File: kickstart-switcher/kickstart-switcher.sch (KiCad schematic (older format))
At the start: 13 parts, among them P1 CONN_01X04, Q1 Q_NMOS_GSD, U1 74HC74, U2 74HC14

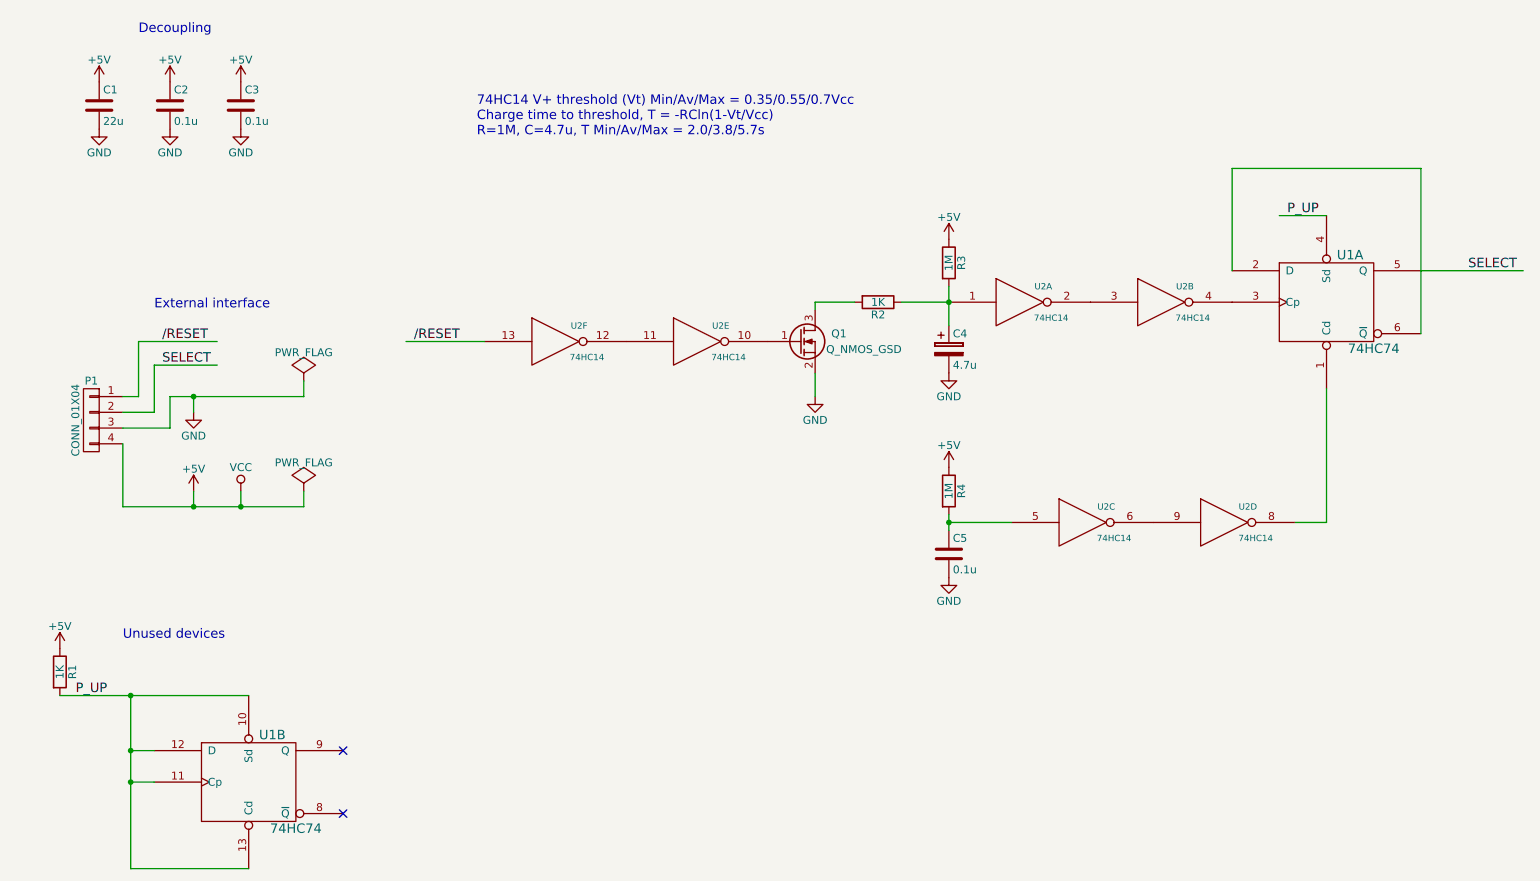
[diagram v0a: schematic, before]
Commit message: kickstart-switcher: Add 1K protection resistors to RC delay HCMOS inputs. Prevents excessive current through over-voltage diodes on power down.
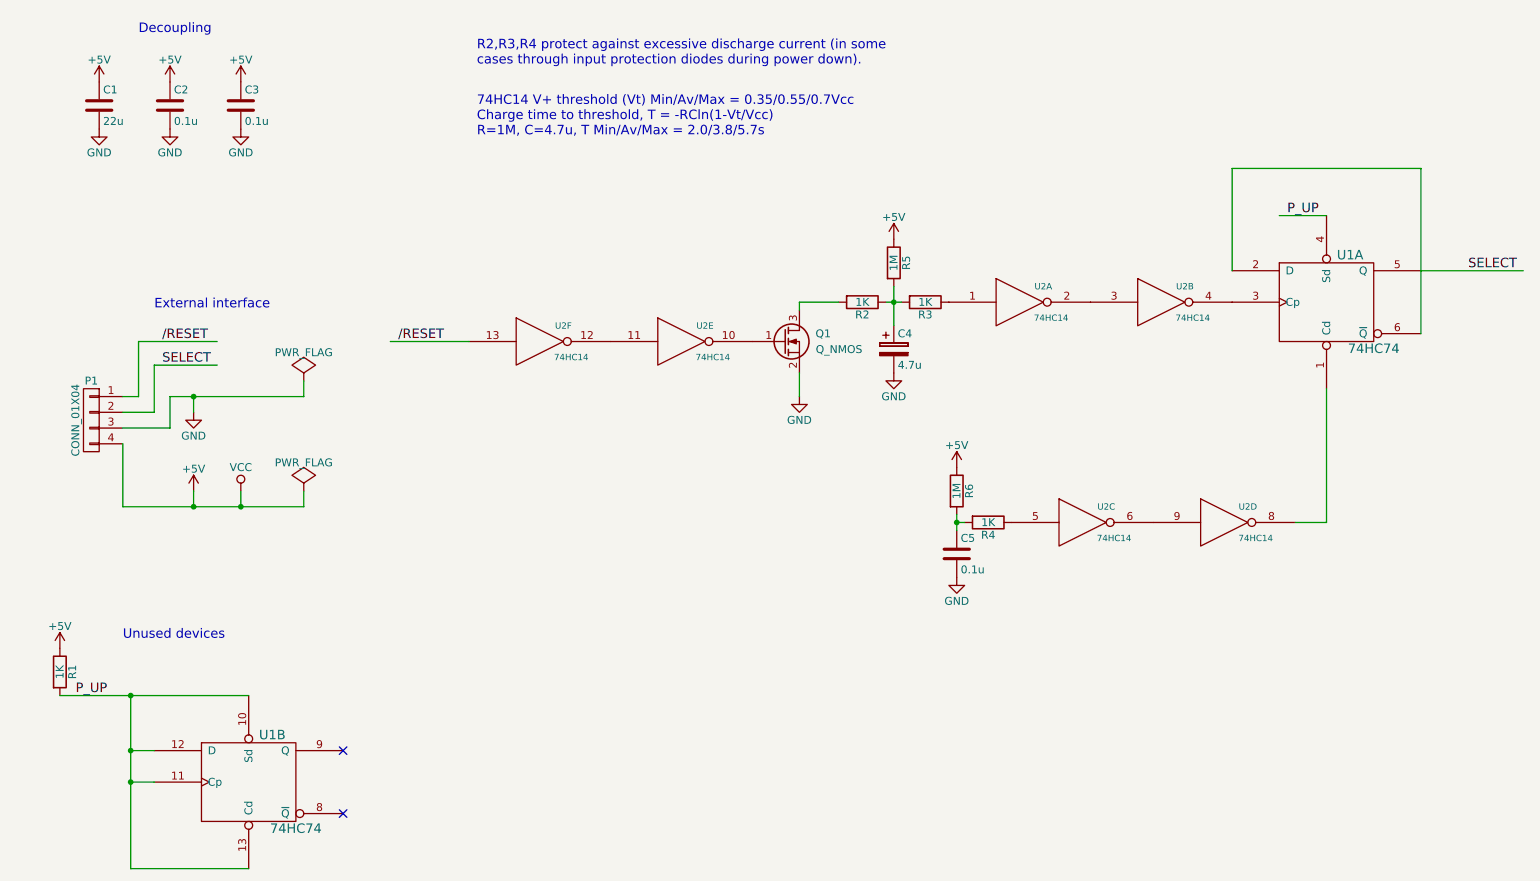
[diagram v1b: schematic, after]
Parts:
- added R3, R4: 1K, Resistors_SMD:R_0805_HandSoldering, symbol R
- Q1: value Q_NMOS_GSD -> Q_NMOS
- renumbered R3 to R5, R4 to R6
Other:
- note added: "R2,R3,R4 protect against excessive discharge current (in some\ncases through input protection diodes during power down)."
- moved on the sheet: C4, C5, Q1, R2, R5, R6, U2E, U2F
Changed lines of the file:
@@
 L +5V #PWR01
 U 1 1 57164698
-P 7150 4250
-F 0 "#PWR01" H 7150 4100 50  0001 C CNN
-F 1 "+5V" H 7150 4390 50  0000 C CNN
-F 2 "" H 7150 4250 60  0000 C CNN
-F 3 "" H 7150 4250 60  0000 C CNN
-	1    7150 4250
+P 7200 4250
+F 0 "#PWR01" H 7200 4100 50  0001 C CNN
+F 1 "+5V" H 7200 4390 50  0000 C CNN
+F 2 "" H 7200 4250 60  0000 C CNN
+F 3 "" H 7200 4250 60  0000 C CNN
+	1    7200 4250
 	1    0    0    -1
 $EndComp
@@
 L GND #PWR02
 U 1 1 571646AB
-P 7150 4950
-F 0 "#PWR02" H 7150 4700 50  0001 C CNN
-F 1 "GND" H 7150 4800 50  0000 C CNN
-F 2 "" H 7150 4950 60  0000 C CNN
-F 3 "" H 7150 4950 60  0000 C CNN
-	1    7150 4950
+P 7200 4950
+F 0 "#PWR02" H 7200 4700 50  0001 C CNN
+F 1 "GND" H 7200 4800 50  0000 C CNN
+F 2 "" H 7200 4950 60  0000 C CNN
+F 3 "" H 7200 4950 60  0000 C CNN
+	1    7200 4950
 	1    0    0    -1
 $EndComp
@@
 L GND #PWR03
 U 1 1 57164A5D
-P 6300 3800
-F 0 "#PWR03" H 6300 3550 50  0001 C CNN
-F 1 "GND" H 6300 3650 50  0000 C CNN
-F 2 "" H 6300 3800 60  0000 C CNN
-F 3 "" H 6300 3800 60  0000 C CNN
-	1    6300 3800
-	1    0    0    -1
-$EndComp
-$Comp
-L R R4
+P 6200 3800
+F 0 "#PWR03" H 6200 3550 50  0001 C CNN
+F 1 "GND" H 6200 3650 50  0000 C CNN
+F 2 "" H 6200 3800 60  0000 C CNN
+F 3 "" H 6200 3800 60  0000 C CNN
+	1    6200 3800
+	1    0    0    -1
+$EndComp
+$Comp
+L R R6
 U 1 1 57164D81
-P 7150 4400
-F 0 "R4" V 7230 4400 50  0000 C CNN
-F 1 "1M" V 7150 4400 50  0000 C CNN
-F 2 "Resistors_SMD:R_0805_HandSoldering" V 7080 4400 30  0001 C CNN
-F 3 "" H 7150 4400 30  0000 C CNN
-	1    7150 4400
+P 7200 4400
+F 0 "R6" V 7280 4400 50  0000 C CNN
+F 1 "1M" V 7200 4400 50  0000 C CNN
+F 2 "Resistors_SMD:R_0805_HandSoldering" V 7130 4400 30  0001 C CNN
+F 3 "" H 7200 4400 30  0000 C CNN
+	1    7200 4400
 	1    0    0    -1
 $EndComp
@@
 L C C5
 U 1 1 57164DA8
-P 7150 4800
-F 0 "C5" H 7175 4900 50  0000 L CNN
-F 1 "0.1u" H 7175 4700 50  0000 L CNN
-F 2 "Resistors_SMD:R_0805_HandSoldering" H 7188 4650 30  0001 C CNN
-F 3 "" H 7150 4800 60  0000 C CNN
-	1    7150 4800
+P 7200 4800
+F 0 "C5" H 7225 4900 50  0000 L CNN
+F 1 "0.1u" H 7225 4700 50  0000 L CNN
+F 2 "Resistors_SMD:R_0805_HandSoldering" H 7238 4650 30  0001 C CNN
+F 3 "" H 7200 4800 60  0000 C CNN
+	1    7200 4800
 	1    0    0    -1
 $EndComp
@@
 L CP C4
 U 1 1 57164E15
-P 7150 3500
-F 0 "C4" H 7175 3600 50  0000 L CNN
-F 1 "4.7u" H 7175 3400 50  0000 L CNN
-F 2 "Resistors_SMD:R_0805_HandSoldering" H 7188 3350 30  0001 C CNN
-F 3 "" H 7150 3500 60  0000 C CNN
-	1    7150 3500
-	1    0    0    -1
-$EndComp
-$Comp
-L R R3
+P 6800 3500
+F 0 "C4" H 6825 3600 50  0000 L CNN
+F 1 "4.7u" H 6825 3400 50  0000 L CNN
+F 2 "Resistors_SMD:R_0805_HandSoldering" H 6838 3350 30  0001 C CNN
+F 3 "" H 6800 3500 60  0000 C CNN
+	1    6800 3500
+	1    0    0    -1
+$EndComp
+$Comp
+L R R5
 U 1 1 57164E66
-P 7150 2950
-F 0 "R3" V 7230 2950 50  0000 C CNN
-F 1 "1M" V 7150 2950 50  0000 C CNN
-F 2 "Resistors_SMD:R_0805_HandSoldering" V 7080 2950 30  0001 C CNN
-F 3 "" H 7150 2950 30  0000 C CNN
-	1    7150 2950
+P 6800 2950
+F 0 "R5" V 6880 2950 50  0000 C CNN
+F 1 "1M" V 6800 2950 50  0000 C CNN
+F 2 "Resistors_SMD:R_0805_HandSoldering" V 6730 2950 30  0001 C CNN
+F 3 "" H 6800 2950 30  0000 C CNN
+	1    6800 2950
 	1    0    0    -1
 $EndComp
@@
 L +5V #PWR04
 U 1 1 57164F16
-P 7150 2800
-F 0 "#PWR04" H 7150 2650 50  0001 C CNN
-F 1 "+5V" H 7150 2940 50  0000 C CNN
-F 2 "" H 7150 2800 60  0000 C CNN
-F 3 "" H 7150 2800 60  0000 C CNN
-	1    7150 2800
+P 6800 2800
+F 0 "#PWR04" H 6800 2650 50  0001 C CNN
+F 1 "+5V" H 6800 2940 50  0000 C CNN
+F 2 "" H 6800 2800 60  0000 C CNN
+F 3 "" H 6800 2800 60  0000 C CNN
+	1    6800 2800
 	1    0    0    -1
 $EndComp
@@
 L GND #PWR05
 U 1 1 57164F39
-P 7150 3650
-F 0 "#PWR05" H 7150 3400 50  0001 C CNN
-F 1 "GND" H 7150 3500 50  0000 C CNN
-F 2 "" H 7150 3650 60  0000 C CNN
-F 3 "" H 7150 3650 60  0000 C CNN
-	1    7150 3650
+P 6800 3650
+F 0 "#PWR05" H 6800 3400 50  0001 C CNN
+F 1 "GND" H 6800 3500 50  0000 C CNN
+F 2 "" H 6800 3650 60  0000 C CNN
+F 3 "" H 6800 3650 60  0000 C CNN
+	1    6800 3650
 	1    0    0    -1
 $EndComp
@@
 NoConn ~ 3300 6050
 NoConn ~ 3300 6450
-Text Label 3750 3450 0    60   ~ 0
+Text Label 3650 3450 0    60   ~ 0
 /RESET
 Text Label 10450 3000 0    60   ~ 0
@@
 $EndComp
 Wire Wire Line
-	7150 4550 7150 4650
-Wire Wire Line
-	7150 4600 7550 4600
-Connection ~ 7150 4600
-Wire Wire Line
-	6300 3650 6300 3800
-Wire Wire Line
-	7150 3100 7150 3350
-Connection ~ 7150 3200
+	7200 4550 7200 4650
+Connection ~ 7200 4600
+Wire Wire Line
+	6200 3650 6200 3800
+Wire Wire Line
+	6800 3100 6800 3350
+Connection ~ 6800 3200
 Wire Wire Line
 	1950 6800 2700 6800
@@
 	9550 2650 9250 2650
 Wire Wire Line
-	4200 3450 3700 3450
+	4100 3450 3600 3450
 Wire Wire Line
 	10150 3000 10800 3000
@@
 L Q_NMOS_GSD Q1
 U 1 1 57188628
-P 6200 3450
-F 0 "Q1" H 6500 3500 50  0000 R CNN
-F 1 "Q_NMOS_GSD" H 6850 3400 50  0000 R CNN
-F 2 "TO_SOT_Packages_SMD:SOT-23_Handsoldering" H 6400 3550 29  0001 C CNN
-F 3 "" H 6200 3450 60  0000 C CNN
-	1    6200 3450
+P 6100 3450
+F 0 "Q1" H 6400 3500 50  0000 R CNN
+F 1 "Q_NMOS" H 6600 3400 50  0000 R CNN
+F 2 "TO_SOT_Packages_SMD:SOT-23_Handsoldering" H 6300 3550 29  0001 C CNN
+F 3 "" H 6100 3450 60  0000 C CNN
+	1    6100 3450
 	1    0    0    -1
 $EndComp
@@
 L R R2
 U 1 1 57188766
-P 6700 3200
-F 0 "R2" V 6780 3200 50  0000 C CNN
-F 1 "1K" V 6700 3200 50  0000 C CNN
-F 2 "Resistors_SMD:R_0805_HandSoldering" V 6630 3200 30  0001 C CNN
-F 3 "" H 6700 3200 30  0000 C CNN
-	1    6700 3200
+P 6600 3200
+F 0 "R2" V 6680 3200 50  0000 C CNN
+F 1 "1K" V 6600 3200 50  0000 C CNN
+F 2 "Resistors_SMD:R_0805_HandSoldering" V 6530 3200 30  0001 C CNN
+F 3 "" H 6600 3200 30  0000 C CNN
+	1    6600 3200
 	0    1    1    0
 $EndComp
 Wire Wire Line
-	6300 3250 6300 3200
-Wire Wire Line
-	6300 3200 6550 3200
+	6200 3250 6200 3200
+Wire Wire Line
+	6200 3200 6450 3200
 $Comp
 L 74HC14 U2
@@
 	1    0    0    -1
 $EndComp
-Wire Wire Line
-	6850 3200 7150 3200
 $Comp
 L 74HC14 U2
@@
 L 74HC14 U2
 U 6 1 571894A7
-P 4650 3450
-F 0 "U2" H 4800 3550 40  0000 C CNN
-F 1 "74HC14" H 4850 3350 40  0000 C CNN
-F 2 "SMD_Packages:SOIC-14_N" H 4650 3450 60  0001 C CNN
-F 3 "" H 4650 3450 60  0000 C CNN
-	6    4650 3450
+P 4550 3450
+F 0 "U2" H 4700 3550 40  0000 C CNN
+F 1 "74HC14" H 4750 3350 40  0000 C CNN
+F 2 "SMD_Packages:SOIC-14_N" H 4550 3450 60  0001 C CNN
+F 3 "" H 4550 3450 60  0000 C CNN
+	6    4550 3450
 	1    0    0    -1
 $EndComp
@@
 L 74HC14 U2
 U 5 1 57189542
-P 5550 3450
-F 0 "U2" H 5700 3550 40  0000 C CNN
-F 1 "74HC14" H 5750 3350 40  0000 C CNN
-F 2 "SMD_Packages:SOIC-14_N" H 5550 3450 60  0001 C CNN
-F 3 "" H 5550 3450 60  0000 C CNN
-	5    5550 3450
+P 5450 3450
+F 0 "U2" H 5600 3550 40  0000 C CNN
+F 1 "74HC14" H 5650 3350 40  0000 C CNN
+F 2 "SMD_Packages:SOIC-14_N" H 5450 3450 60  0001 C CNN
+F 3 "" H 5450 3450 60  0000 C CNN
+	5    5450 3450
 	1    0    0    -1
 $EndComp
@@
 Wire Wire Line
 	8950 2350 8950 3000
+$Comp
+L R R4
+U 1 1 571A35D1
+P 7400 4600
+F 0 "R4" V 7480 4600 50  0000 C CNN
+F 1 "1K" V 7400 4600 50  0000 C CNN
+F 2 "Resistors_SMD:R_0805_HandSoldering" V 7330 4600 30  0001 C CNN
+F 3 "" H 7400 4600 30  0000 C CNN
+	1    7400 4600
+	0    1    1    0
+$EndComp
+$Comp
+L R R3
+U 1 1 571A3827
+P 7000 3200
+F 0 "R3" V 7080 3200 50  0000 C CNN
+F 1 "1K" V 7000 3200 50  0000 C CNN
+F 2 "Resistors_SMD:R_0805_HandSoldering" V 6930 3200 30  0001 C CNN
+F 3 "" H 7000 3200 30  0000 C CNN
+	1    7000 3200
+	0    1    1    0
+$EndComp
+Wire Wire Line
+	6750 3200 6850 3200
+Wire Wire Line
+	7200 4600 7250 4600
+Text Notes 4150 1700 0    60   ~ 0
+R2,R3,R4 protect against excessive discharge current (in some\ncases through input protection diodes during power down).
 $EndSCHEMATC

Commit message: kickstart-switcher: Use second 74HC74 flip-flop to generate extra select line and allow 4-way image selection
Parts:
- P1: value CONN_01X04 -> CONN_01X05; footprint Pin_Headers:Pin_Header_Straight_1x04 -> Pin_Headers:Pin_Header_Straight_1x05; symbol CONN_01X04 -> CONN_01X05
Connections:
- net labels added: CLR, SEL0, SEL1
- net labels removed: P_UP, SELECT
- wire segments 36 -> 40
- no-connect marks 2 -> 0
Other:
- note added: "Power-Up Clear Flip Flops"
- note removed: "Unused devices"
- moved on the sheet: C4, C5, Q1, R1, R2, R3, R4, R5, R6, U1A, U1B, U2A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
